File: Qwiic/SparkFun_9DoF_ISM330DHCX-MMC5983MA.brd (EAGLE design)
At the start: 25.4 x 25.4 mm, 75 parts, among them J1 QWIIC_RIGHT_ANGLE, J2 QWIIC_RIGHT_ANGLE, U1 ISM330DHCX, U2 MMC5983MA_QFN16

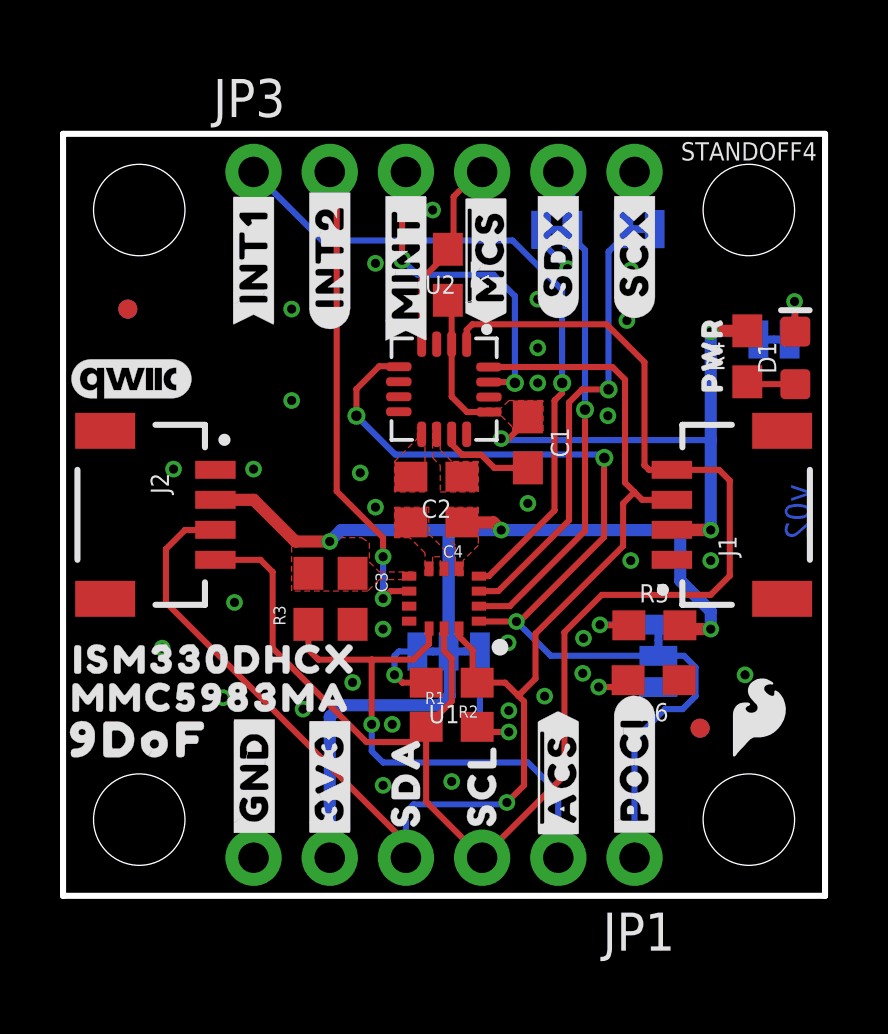
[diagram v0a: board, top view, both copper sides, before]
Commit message: Rolls to v10, adds silk to accelerometer address selection jumper
* Adds note to schematic about magnetometer address not being affected by accelerometer address selection
* Increases size of  VCC and address text
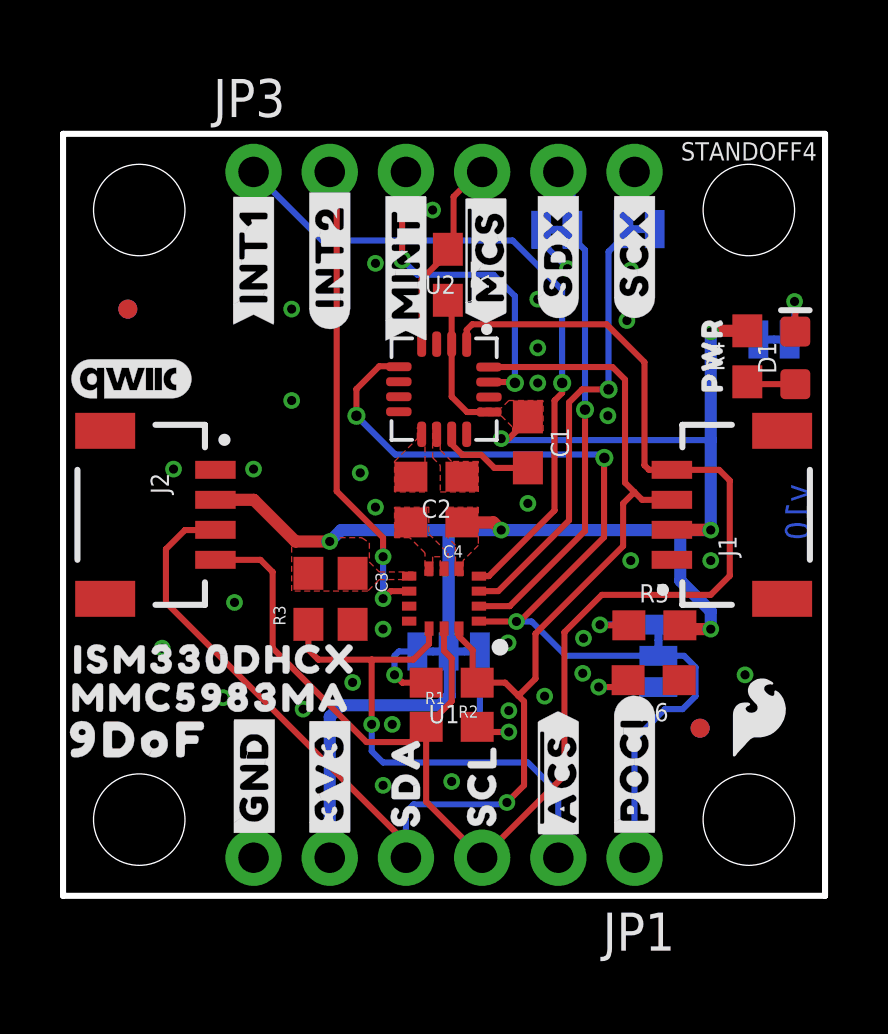
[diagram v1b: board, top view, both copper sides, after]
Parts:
- added U$41: (no value), top:#ACC#17
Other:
- board text added: "v10"
- board text removed: "v02"
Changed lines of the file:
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@@
 <wire x1="0" y1="0" x2="25.4" y2="0" width="0.2032" layer="20"/>
 <wire x1="25.4" y1="0" x2="25.4" y2="25.4" width="0.2032" layer="20"/>
-<text x="24.882475" y="13.725525" size="0.8128" layer="16" font="vector" ratio="22" rot="SMR270">v02</text>
+<text x="24.882475" y="13.725525" size="0.8128" layer="16" font="vector" ratio="22" rot="SMR270">v10</text>
 <wire x1="9.236075" y1="15.1876125" x2="11.141075" y2="15.1876125" width="0.254" layer="22"/>
 <wire x1="10.633075" y1="14.6796125" x2="10.633075" y2="15.8226125" width="0.254" layer="22" curve="-180"/>
@@
 <element name="U$31" library="top" package="#MINT#5" value="" x="11.43" y="21.082" smashed="yes" rot="R90"/>
 <element name="U$34" library="top" package="##MCS##7" value="" x="14.097" y="21.336" smashed="yes" rot="R90"/>
+<element name="U$41" library="top" package="#ACC#17" value="" x="17.399" y="8.128" smashed="yes" rot="MR0"/>
 </elements>
 <signals>
@@
 <wire x1="13.8745" y1="9.144" x2="15.113" y2="9.144" width="0.2032" layer="1"/>
 <via x="15.113" y="9.144" extent="1-16" drill="0.3048"/>
-<wire x1="16.256" y1="8.001" x2="15.113" y2="9.144" width="0.2032" layer="16"/>
-<wire x1="16.256" y1="8.001" x2="19.84375" y2="8.001" width="0.2032" layer="16"/>
+<wire x1="16.764" y1="8.001" x2="15.621" y2="9.144" width="0.2032" layer="16"/>
+<wire x1="15.113" y1="9.144" x2="15.621" y2="9.144" width="0.2032" layer="16"/>
+<wire x1="16.764" y1="8.001" x2="19.84375" y2="8.001" width="0.2032" layer="16"/>
 <wire x1="18.034" y1="11.9534375" x2="15.2245625" y2="9.144" width="0.2032" layer="1"/>
 <wire x1="15.113" y1="9.144" x2="15.2245625" y2="9.144" width="0.2032" layer="1"/>
